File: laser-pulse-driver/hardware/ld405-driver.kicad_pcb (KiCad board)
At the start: 4 copper layers, 160 x 100 mm, 145 parts, among them J1 9V DC IN, J2 TTL IN, J3 SET MON, J4 I MON, J5 LD OUT, J6 INTERLOCK, K1 G6K-2F-Y 5V, Q1 AO3401A, Q10 AO3400A, Q11 AO3401A, Q2 IRFR9024N, Q3 2N7002, Q4 2N7002, Q5 2N7002, Q6 AO3401A, Q7 AO3401A, Q8 2N7002, Q9 2N7002, SW1 ENABLE, U1 L78M05ABDT, U10 TLV9062, U11 LM2901, U12 74HC14, U13 74HC132, U14 74AHCT1G14, U2 REF3030, U3 TLV9062, U4 TLV9062, U5 SN74LVC1G3157, U7 OPA2192, U8 INA180A1

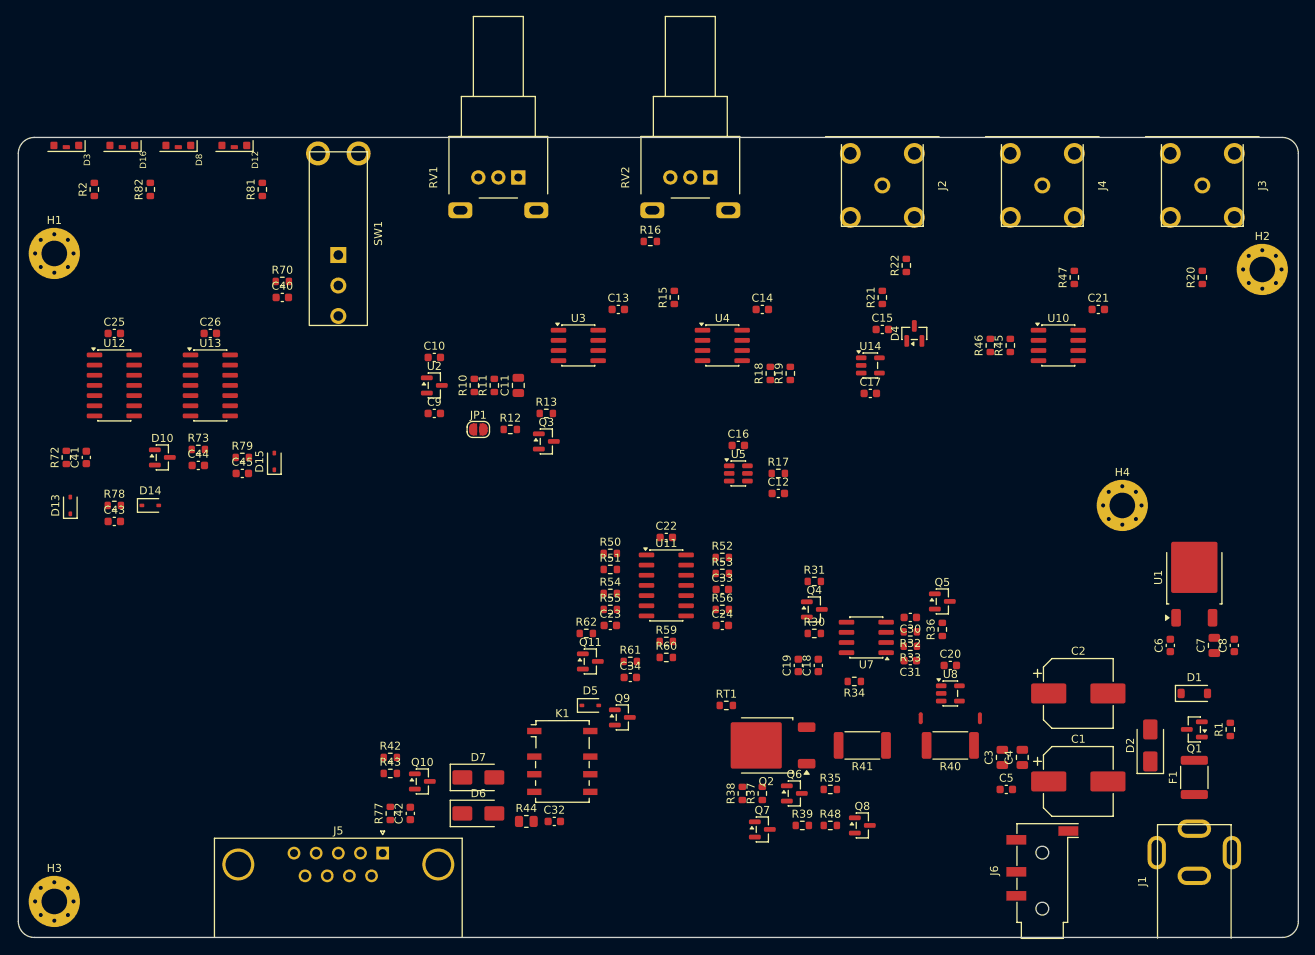
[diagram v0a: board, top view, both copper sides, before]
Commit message: laser-pulse-driver: grid router, routed 4-layer board with planes
Adds a small A* maze router (C core + Python driver) that routes the
board from design.py/placement.py: GND/+5V inner planes with via
fan-outs, tapered wide power paths, Kelvin taps on the sense resistor,
LD_OUT heat spreader with thermal vias, rip-up and retry.  DRC: no
copper violations, no unconnected items, schematic parity clean.

Co-Authored-By: Claude Opus 5.5 <noreply@anthropic.com>
Claude-Session: https://claude.ai/code/session_019RAi5HuganNifeSzFvLjAT
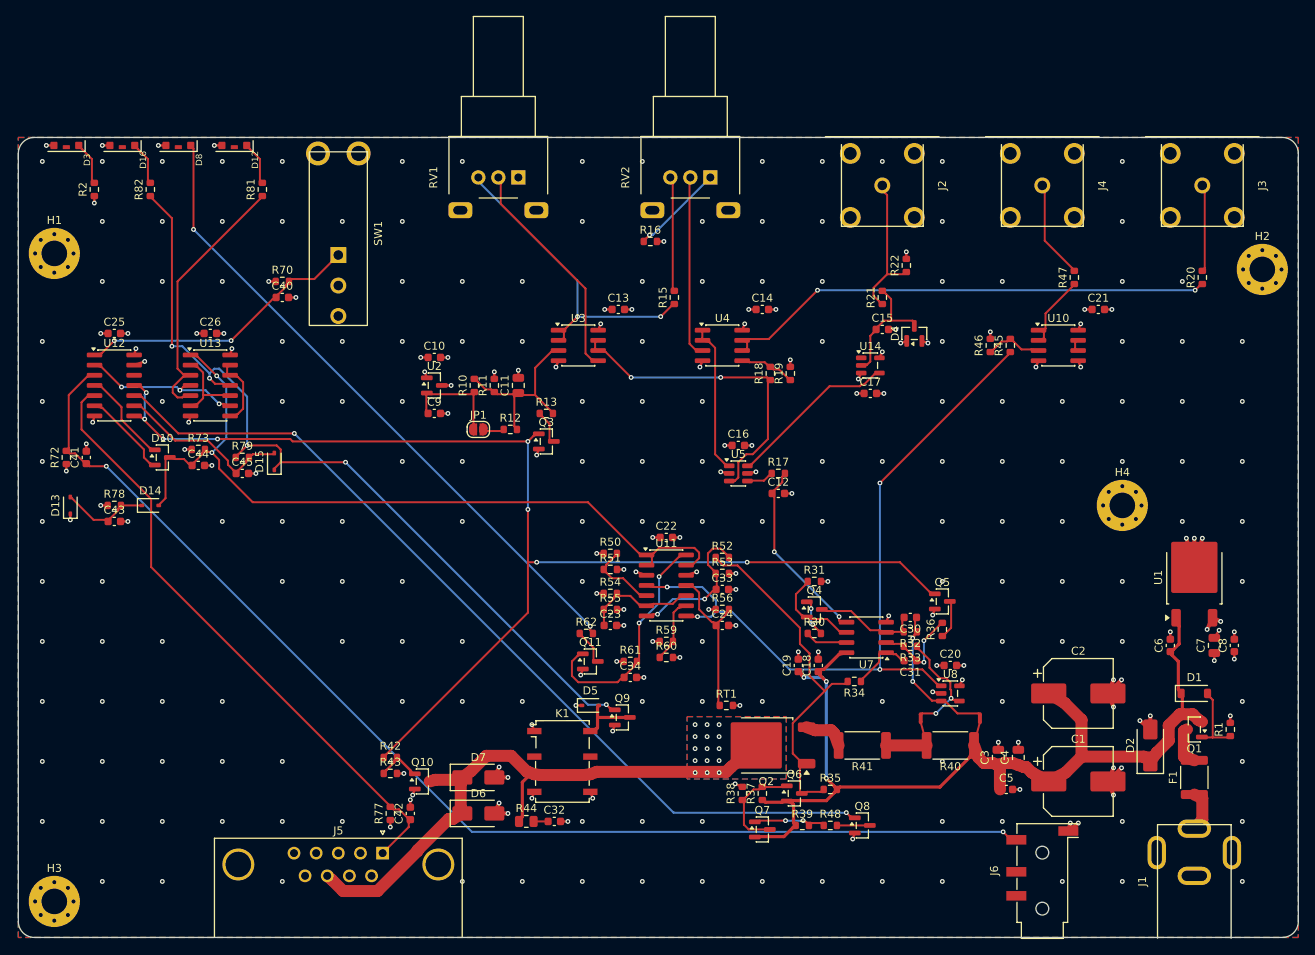
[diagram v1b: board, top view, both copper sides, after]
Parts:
- moved C3 0.50 mm to (222.5, 177.5)
- moved C4 0.50 mm to (225.0, 177.5)
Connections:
- J5 pad 2: (no net) -> unconnected-(J5-Pad2)
- J5 pad 4: (no net) -> unconnected-(J5-Pad4)
- J5 pad 6: (no net) -> unconnected-(J5-Pad6)
- J5 pad 7: (no net) -> unconnected-(J5-Pad7)
- J5 pad 9: (no net) -> unconnected-(J5-Pad9)
- K1 pad 2: (no net) -> unconnected-(K1-Pad2)
- K1 pad 7: (no net) -> unconnected-(K1-Pad7)
- SW1 pad 3: (no net) -> unconnected-(SW1-C-Pad3)
- U12 pad 12: (no net) -> unconnected-(U12-Pad12)
- U14 pad 1: (no net) -> unconnected-(U14-NC-Pad1)
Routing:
- net DIS_LOOP: track 0.00 -> 157.0 mm, vias 0 -> 8
- net REM_N: track 0.00 -> 150.0 mm, vias 0 -> 2
- net VIN: track 0.00 -> 127.0 mm, vias 0 -> 3
- net EN_LOOP: track 0.00 -> 111.8 mm, vias 0 -> 2
- net EN_REQ: track 0.00 -> 105.8 mm, vias 0 -> 5
- net GND: track 0.00 -> 102.0 mm, vias 0 -> 253
- net S_N: track 0.00 -> 100.8 mm, vias 0 -> 2
- net IMON_INT: track 0.00 -> 93.1 mm, vias 0 -> 4
- net LED_EMI: track 0.00 -> 81.8 mm, vias 0 -> 2
- net DB9_IL: track 0.00 -> 77.2 mm
- net LD_OUT: track 0.00 -> 77.2 mm, vias 0 -> 15
- net SETMON_OUT: track 0.00 -> 62.5 mm, vias 0 -> 2
- net GATE: track 0.00 -> 45.5 mm
- net VFS: track 0.00 -> 40.4 mm, vias 0 -> 2
- net VP: track 0.00 -> 40.3 mm, vias 0 -> 2
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- added copper zone on In2.Cu, net +5V
- added copper zone on B.Cu, net GND
- added copper zone on F.Cu, net GND
- added copper zone on In1.Cu, net GND
- added copper zone on B.Cu, net LD_OUT
- added copper zone on F.Cu, net LD_OUT

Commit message: laser-pulse-driver: silkscreen tidy-up, DRC/ERC clean
Reference designators re-placed clear of pads and other silk, footprint
silk trimmed at pads and the board edge, board labels added.  DRC: 0
violations, 0 unconnected, schematic parity clean; ERC: 0.

Co-Authored-By: Claude Opus 5.5 <noreply@anthropic.com>
Claude-Session: https://claude.ai/code/session_019RAi5HuganNifeSzFvLjAT
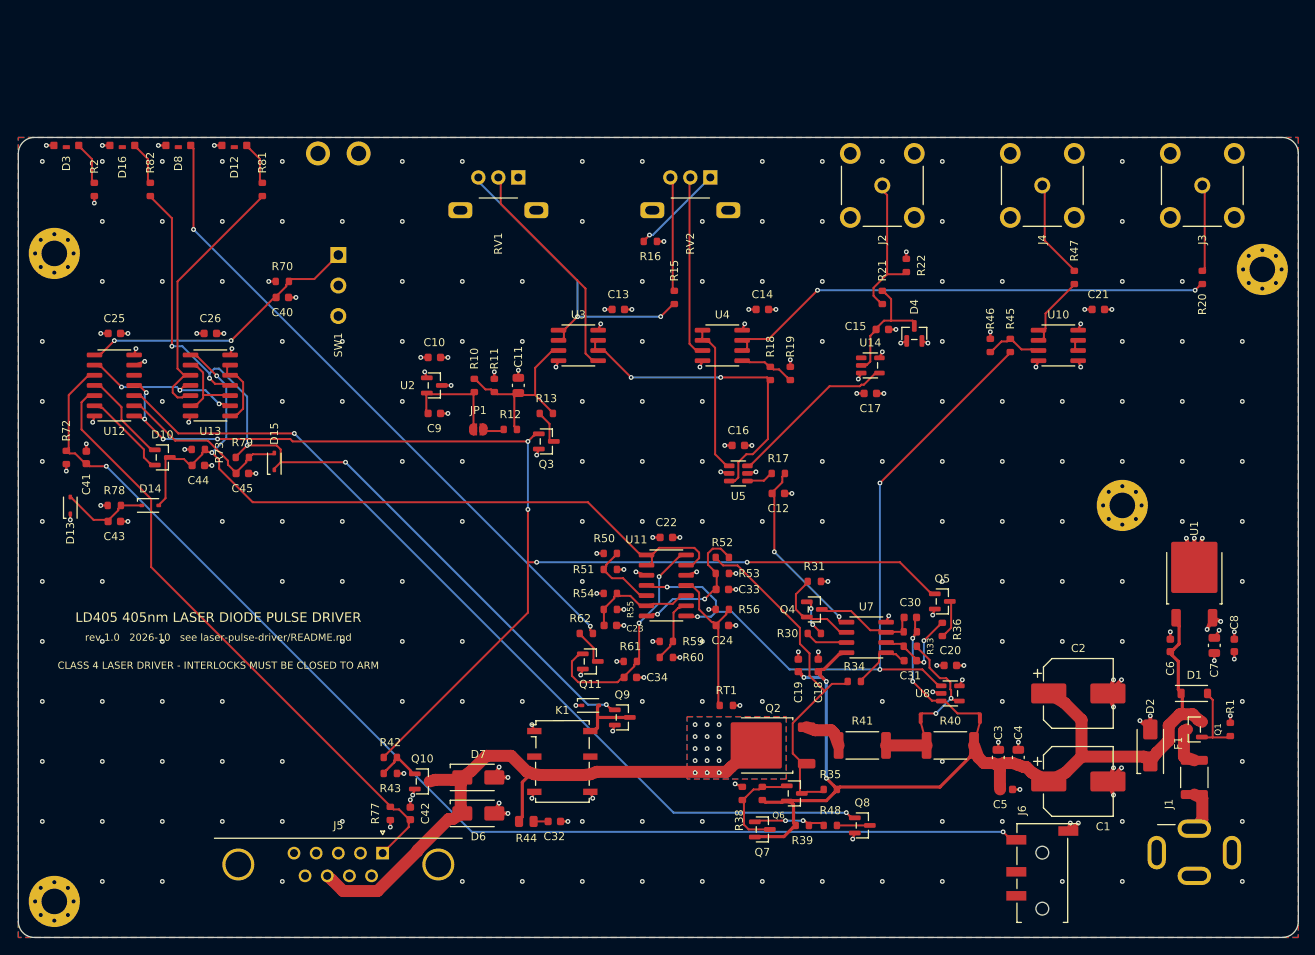
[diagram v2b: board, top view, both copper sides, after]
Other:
- board text added: "CLASS 4 LASER DRIVER - INTERLOCKS MUST BE CLOSED TO ARM"
- board text added: "LD405 405nm LASER DIODE PULSE DRIVER"
- board text added: "rev 1.0 2026-10 see laser-pulse-driver/README.md"
